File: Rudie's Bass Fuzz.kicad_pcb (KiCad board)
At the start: 2 copper layers, 25 x 50 mm, 13 parts, among them J1 Conn_01x01_Male, J2 Conn_01x01_Male, J3 Conn_01x01_Male, J4 Conn_01x01_Male, Q1 BC549

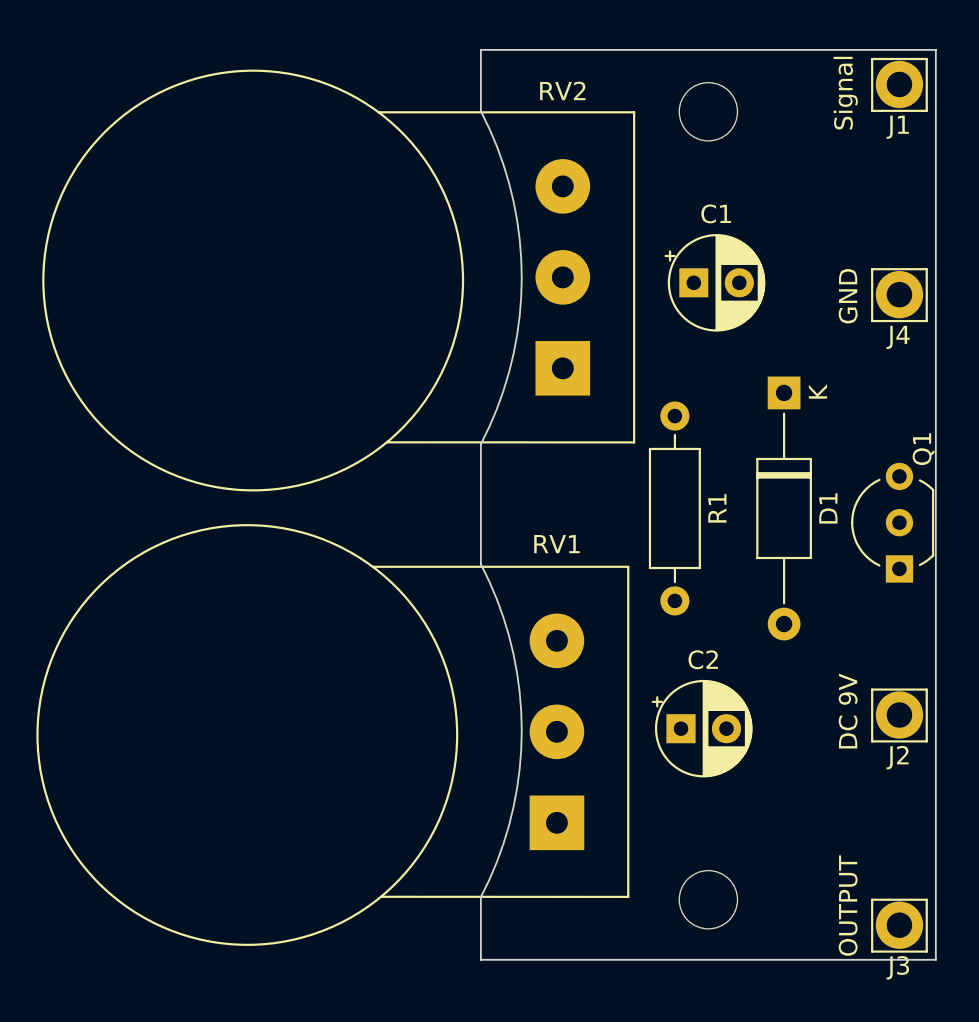
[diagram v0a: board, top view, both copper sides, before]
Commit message: aligned components
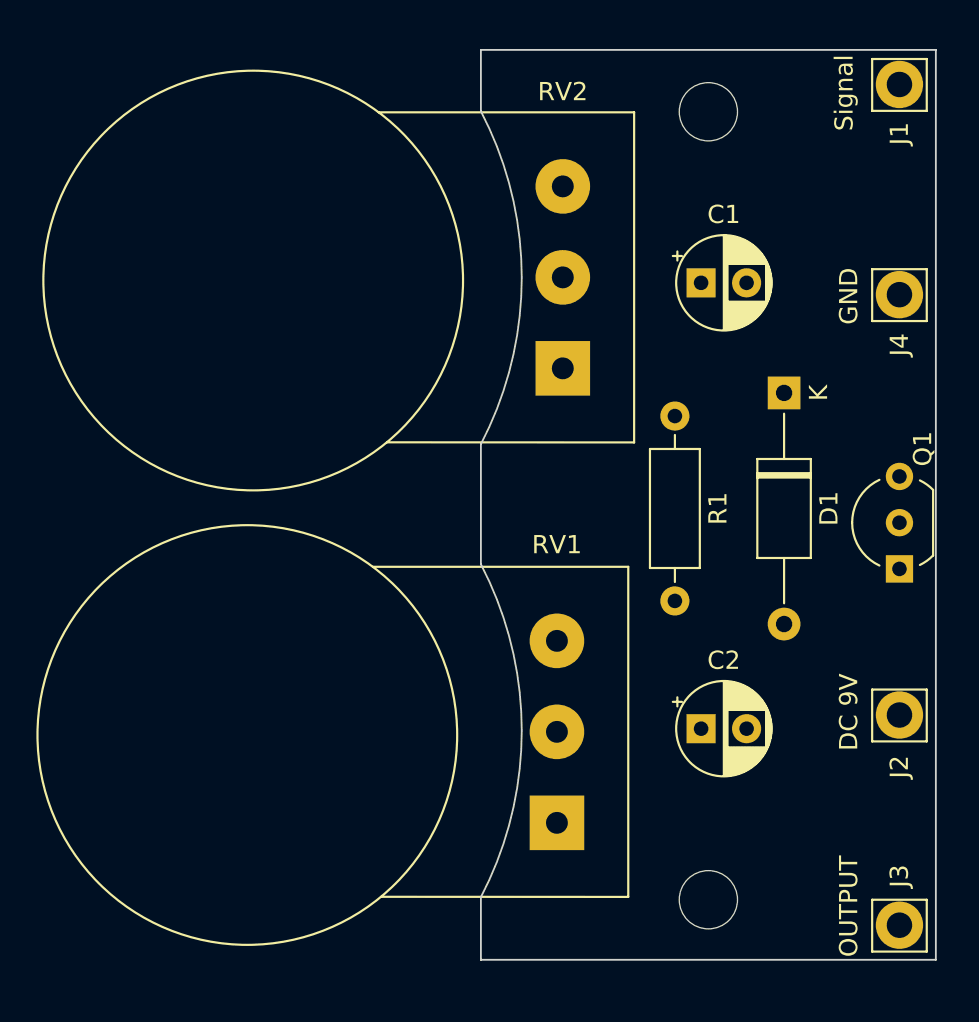
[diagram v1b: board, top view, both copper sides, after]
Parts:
- moved C2 1.11 mm to (170.7, 79.9)
- moved C1 0.40 mm to (170.7, 55.4)
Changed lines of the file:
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@@
     (property "Sheetname" "")
     (attr through_hole)
-    (fp_text reference "J1" (at 0 2.25) (layer "F.SilkS")
+    (fp_text reference "J1" (at 0 2.7 90) (layer "F.SilkS")
       (effects (font (size 1 1) (thickness 0.15)))
     )
@@
   )
   (footprint "Capacitor_THT:CP_Radial_D5.0mm_P2.50mm" (layer "F.Cu")
-    (at 169.594888 79.9)
+    (at 170.7 79.9)
     (descr "CP, Radial series, Radial, pin pitch=2.50mm, , diameter=5mm, Electrolytic Capacitor")
     (tags "CP Radial series Radial pin pitch 2.50mm  diameter 5mm Electrolytic Capacitor")
@@
     (property "Sheetname" "")
     (attr through_hole)
-    (fp_text reference "J2" (at 0 2.25) (layer "F.SilkS")
+    (fp_text reference "J2" (at 0 2.85 270) (layer "F.SilkS")
       (effects (font (size 1 1) (thickness 0.15)))
     )
@@
     (property "Sheetname" "")
     (attr through_hole)
-    (fp_text reference "J4" (at 0 2.25) (layer "F.SilkS")
+    (fp_text reference "J4" (at 0 2.75 90) (layer "F.SilkS")
       (effects (font (size 1 1) (thickness 0.15)))
     )
@@
   )
   (footprint "Capacitor_THT:CP_Radial_D5.0mm_P2.50mm" (layer "F.Cu")
-    (at 170.3 55.4)
+    (at 170.7 55.4)
     (descr "CP, Radial series, Radial, pin pitch=2.50mm, , diameter=5mm, Electrolytic Capacitor")
     (tags "CP Radial series Radial pin pitch 2.50mm  diameter 5mm Electrolytic Capacitor")
@@
     (property "Sheetname" "")
     (attr through_hole)
-    (fp_text reference "J3" (at 0 2.25) (layer "F.SilkS")
-      (effects (font (size 1 1) (thickness 0.15)))
-    )
+    (fp_text reference "J3" (at 0 -2.7 90) (layer "F.SilkS")
+      (effects (font (size 1 1) (thickness 0.15)))
+    )
